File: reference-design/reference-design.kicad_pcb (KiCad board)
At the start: 2 copper layers, 69.5 x 38.2 mm, 21 parts

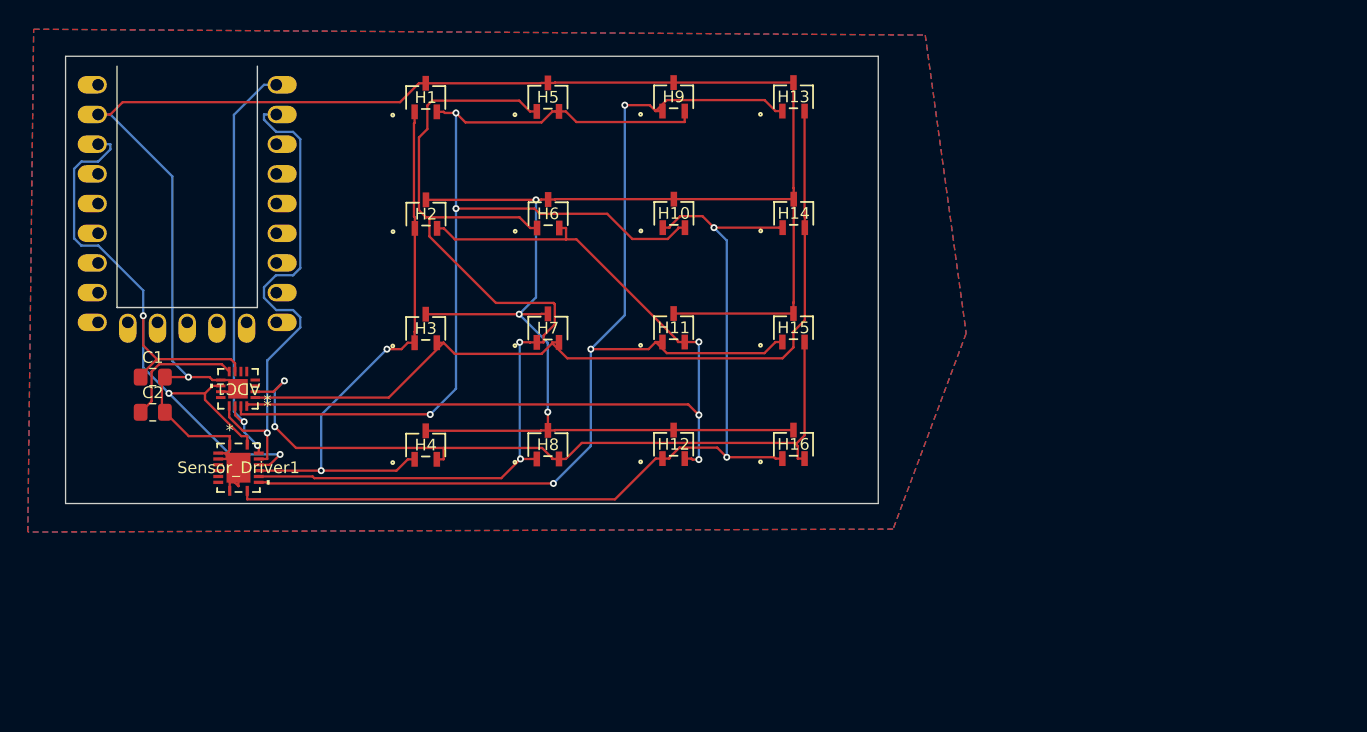
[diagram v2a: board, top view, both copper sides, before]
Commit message: fix thermal vias
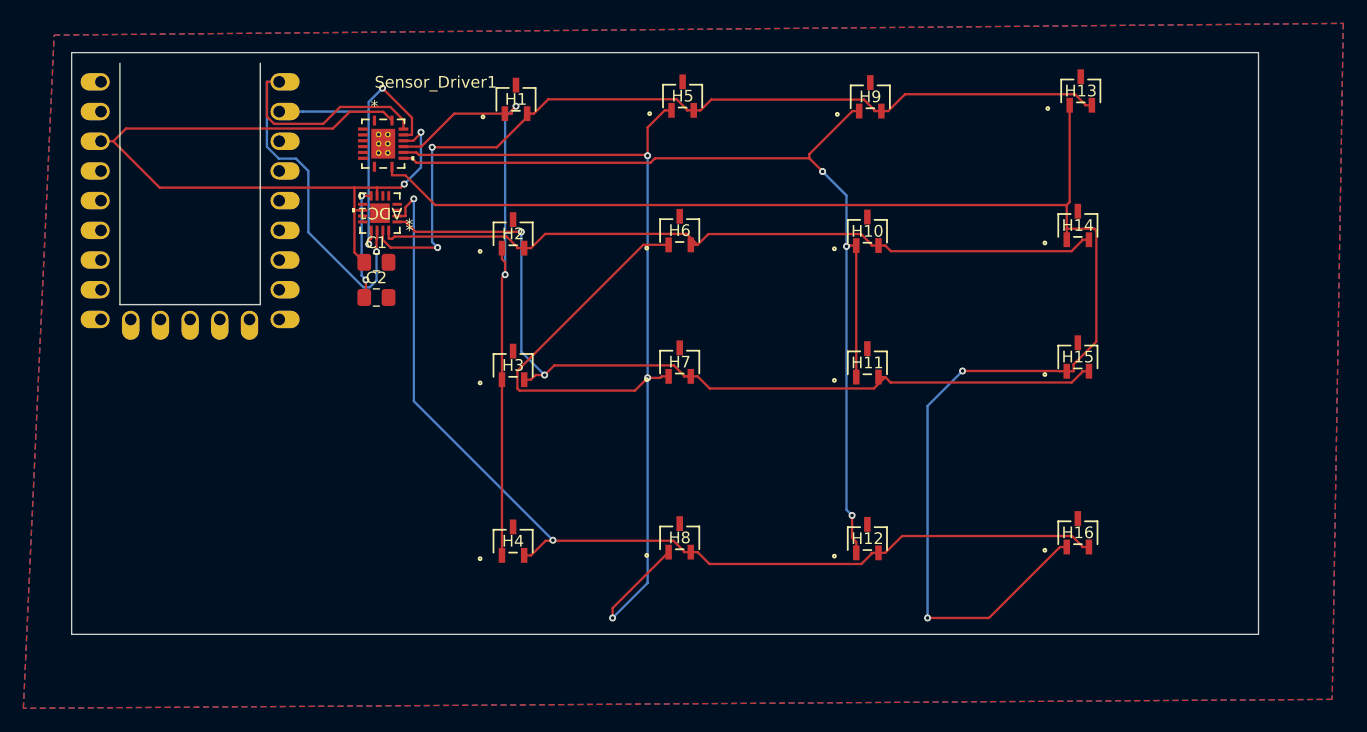
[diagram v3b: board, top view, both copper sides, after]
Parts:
- moved Sensor_Driver1 30.4 mm to (39.1, 19.5)
- moved H16 25.5 mm to (98.5, 52.8)
- moved H13 24.6 mm to (98.8, 15.0)
- moved H15 24.4 mm to (98.5, 37.8)
- moved H14 24.3 mm to (98.5, 26.5)
- moved C1 21.5 mm to (38.6, 29.7)
- moved C2 21.5 mm to (38.6, 32.7)
- moved ADC1 19.3 mm to (38.9, 25.5)
- moved H12 18.4 mm to (80.5, 53.3)
- moved H11 16.8 mm to (80.5, 38.3)
- moved H9 16.8 mm to (80.8, 15.5)
- moved H10 16.6 mm to (80.5, 27.0)
- moved H8 13.8 mm to (64.5, 53.2)
- moved H7 11.6 mm to (64.5, 38.2)
- moved H5 11.5 mm to (64.8, 15.5)
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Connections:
- H10 pad 1: row3 -> row2
- H10 pad 2: col0 -> col1
- H11 pad 2: col1 -> col2
- H12 pad 1: row3 -> row2
- H12 pad 2: col1 -> col3
- H13 pad 1: row2 -> row3
- H13 pad 2: col2 -> col0
- H14 pad 2: col2 -> col1
- H15 pad 1: row2 -> row3
- H15 pad 2: col3 -> col2
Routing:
- net GND: track 237.9 -> 0.00 mm, vias 4 -> 0
- net row3: track 79.9 -> 132.8 mm
- net row1: track 84.9 -> 106.8 mm, vias 2 -> 3
- net col3: track 66.0 -> 87.8 mm
- net i2c0_scl: track 43.6 -> 28.5 mm, vias 1 -> 2
- net col1: track 78.4 -> 64.1 mm, vias 3 -> 0
- net col0: track 88.0 -> 75.3 mm, vias 3 -> 2
- net i2c0_sda: track 36.3 -> 46.4 mm, vias 2 -> 1
- net row2: track 93.2 -> 88.7 mm
- net col2: track 71.5 -> 75.3 mm, vias 0 -> 2
- net row0: track 48.9 -> 52.5 mm
- net Net-(ADC1-DECAP): track 11.0 -> 9.73 mm, vias 0 -> 2
- net +3.3V: track 67.3 -> 67.9 mm, vias 3 -> 2
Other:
- board size 69.5 x 38.2 mm -> 101.5 x 49.8 mm

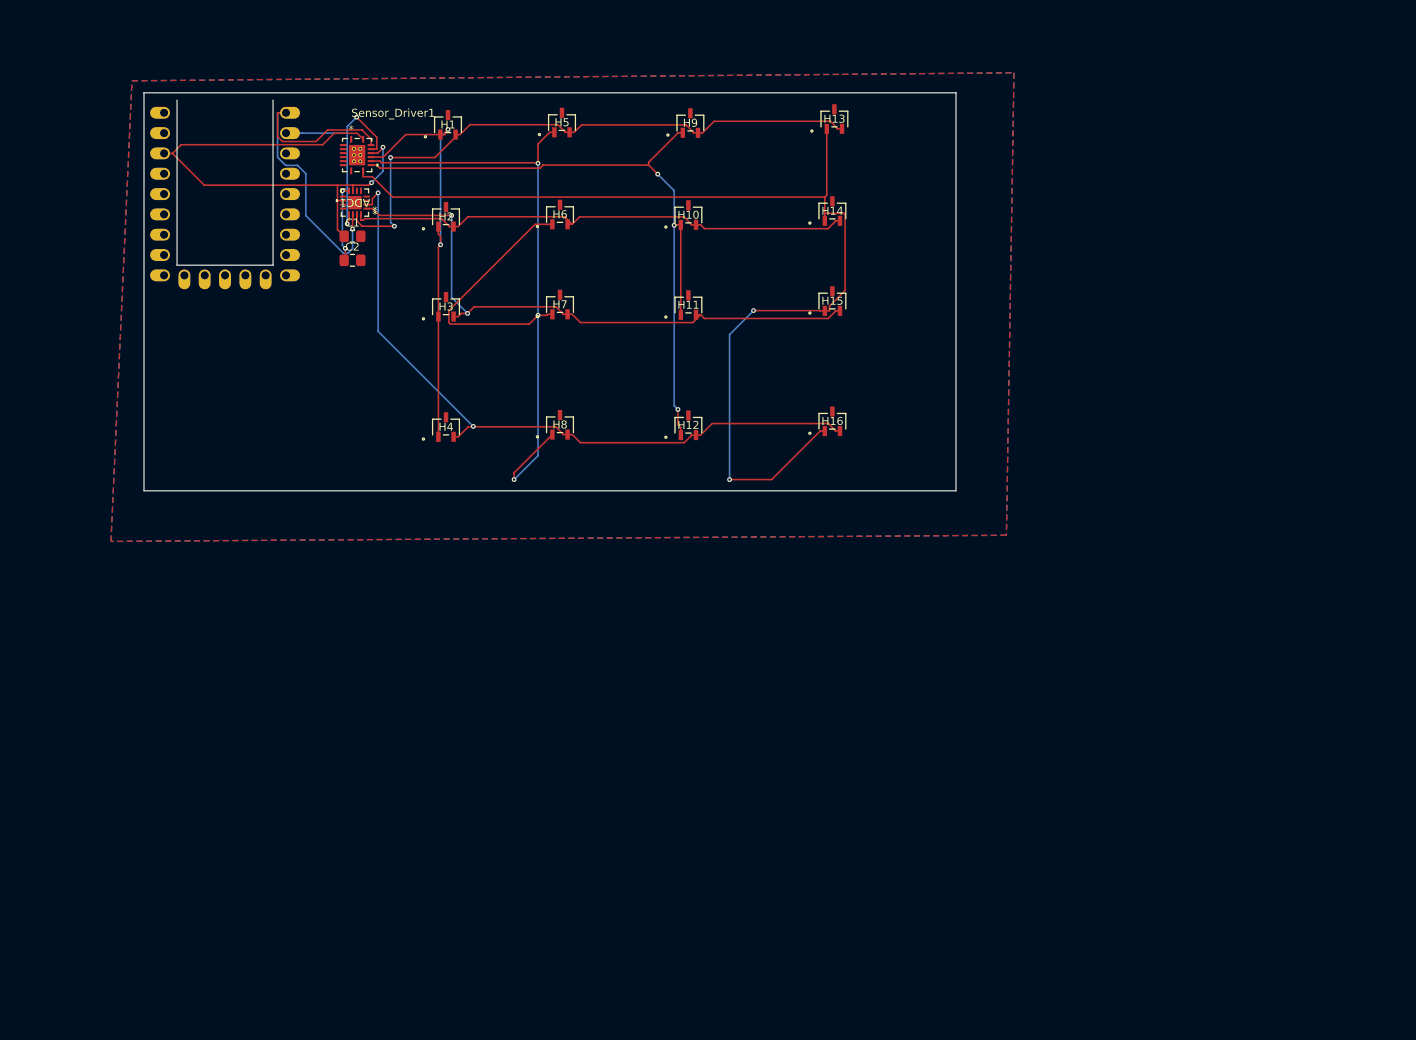
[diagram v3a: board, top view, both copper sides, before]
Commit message: add keyb outlines and rearrange grid
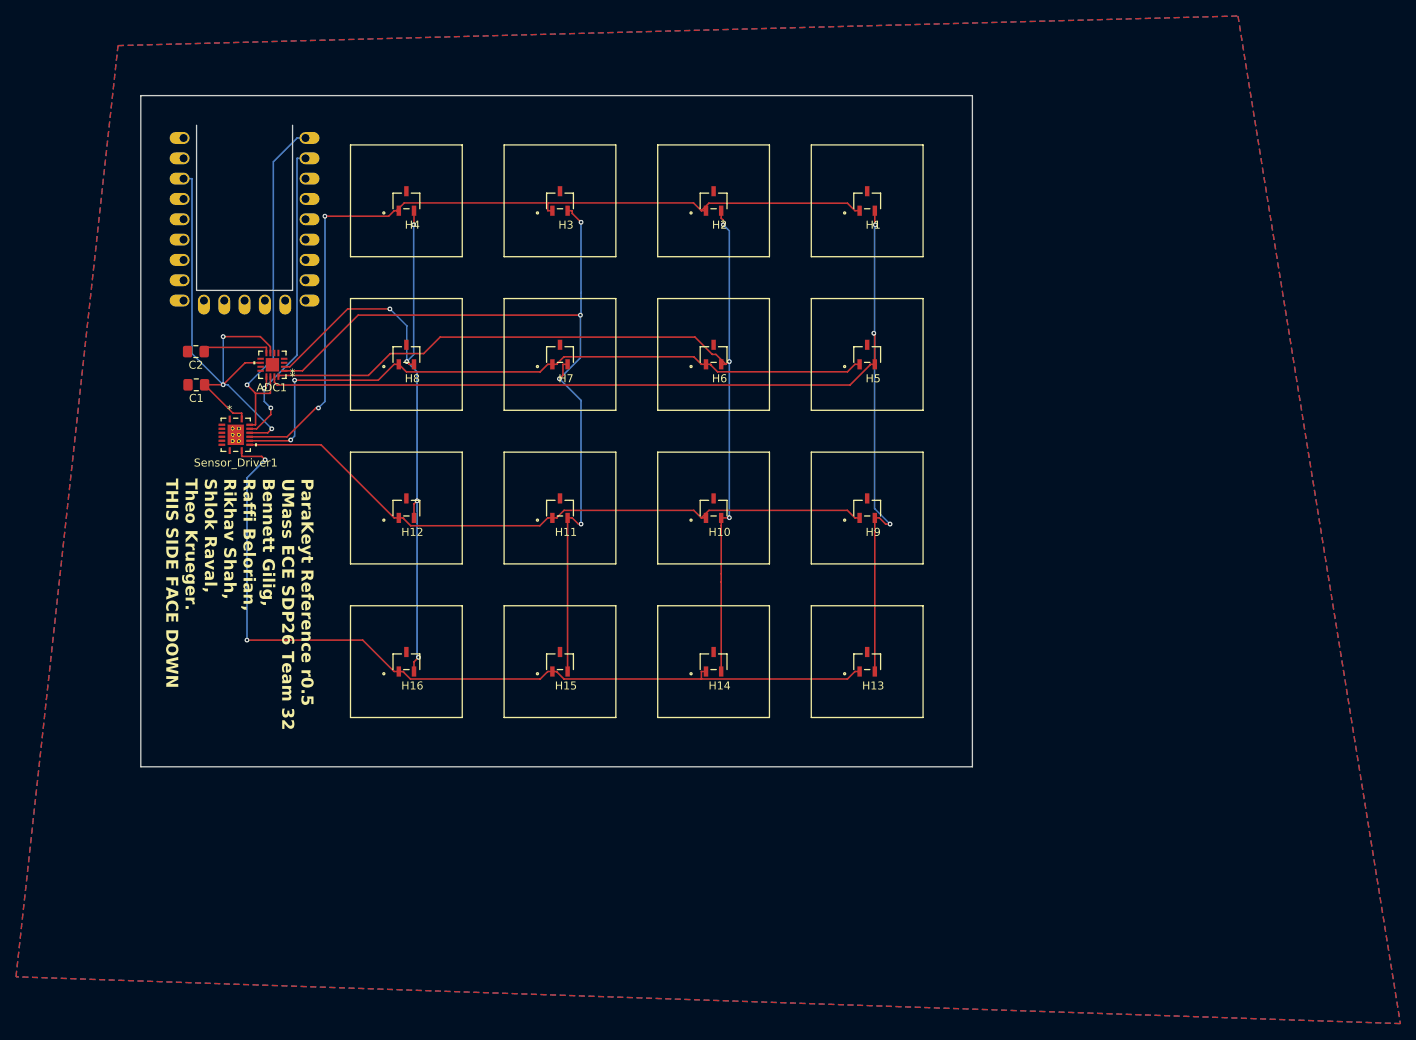
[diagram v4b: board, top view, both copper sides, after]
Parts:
- H1, H10, H11, H12, H13, H14, H15, H16, H2, H3, H4, H5, H6, H7, H8, H9: footprint AH49FNTR_G1:SC59_DIO -> AH49FNTR_G1:SC59_DIO_KeyswitchOutline
- moved H13 67.9 mm to (102.9, 82.8)
- moved H16 61.2 mm to (45.3, 82.8)
- moved H14 58.2 mm to (83.7, 82.8)
- moved H15 56.5 mm to (64.5, 82.8)
- moved H1 53.2 mm to (102.9, 25.2)
- moved H9 52.9 mm to (102.9, 63.6)
- moved H5 47.9 mm to (102.9, 44.4)
- moved Sensor_Driver1 38.1 mm to (24.0, 54.5)
- moved H12 36.8 mm to (45.3, 63.6)
- moved H10 36.7 mm to (83.7, 63.6)
- moved H2 33.5 mm to (83.7, 25.2)
- moved H11 30.0 mm to (64.5, 63.6)
- moved H4 28.7 mm to (45.3, 25.2)
- moved C1 26.9 mm to (19.0, 48.2), turned to 180 degrees
- moved H6 25.9 mm to (83.7, 44.4)
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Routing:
- net col0: track 75.3 -> 142.5 mm, vias 2 -> 3
- net col1: track 64.1 -> 119.6 mm, vias 0 -> 3
- net row0: track 52.5 -> 105.5 mm
- net col2: track 75.3 -> 106.2 mm, vias 2 -> 4
- net row3: track 132.8 -> 108.7 mm
- net row1: track 106.8 -> 86.7 mm, vias 3 -> 2
- net i2c0_scl: track 28.5 -> 40.1 mm
- net row2: track 88.7 -> 83.1 mm, vias 3 -> 0
- net col3: track 87.8 -> 85.8 mm, vias 2 -> 5
- net i2c0_sda: track 46.4 -> 44.6 mm
- net Net-(ADC1-DECAP): track 9.73 -> 8.70 mm, vias 2 -> 0
- net +3.3V: track 67.9 -> 68.0 mm, vias 2 -> 3
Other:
- board size 101.5 x 49.8 mm -> 104 x 83.9 mm
- board text added: "ParaKeyt Reference r0.5 UMass ECE SDP26 Team 32 Bennett Gilig, Raffi Belorian, Rikhav Shah, Shlok Raval, Theo Krueger. THIS SIDE FACE DOWN"
